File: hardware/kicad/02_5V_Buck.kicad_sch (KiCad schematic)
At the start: 9 parts

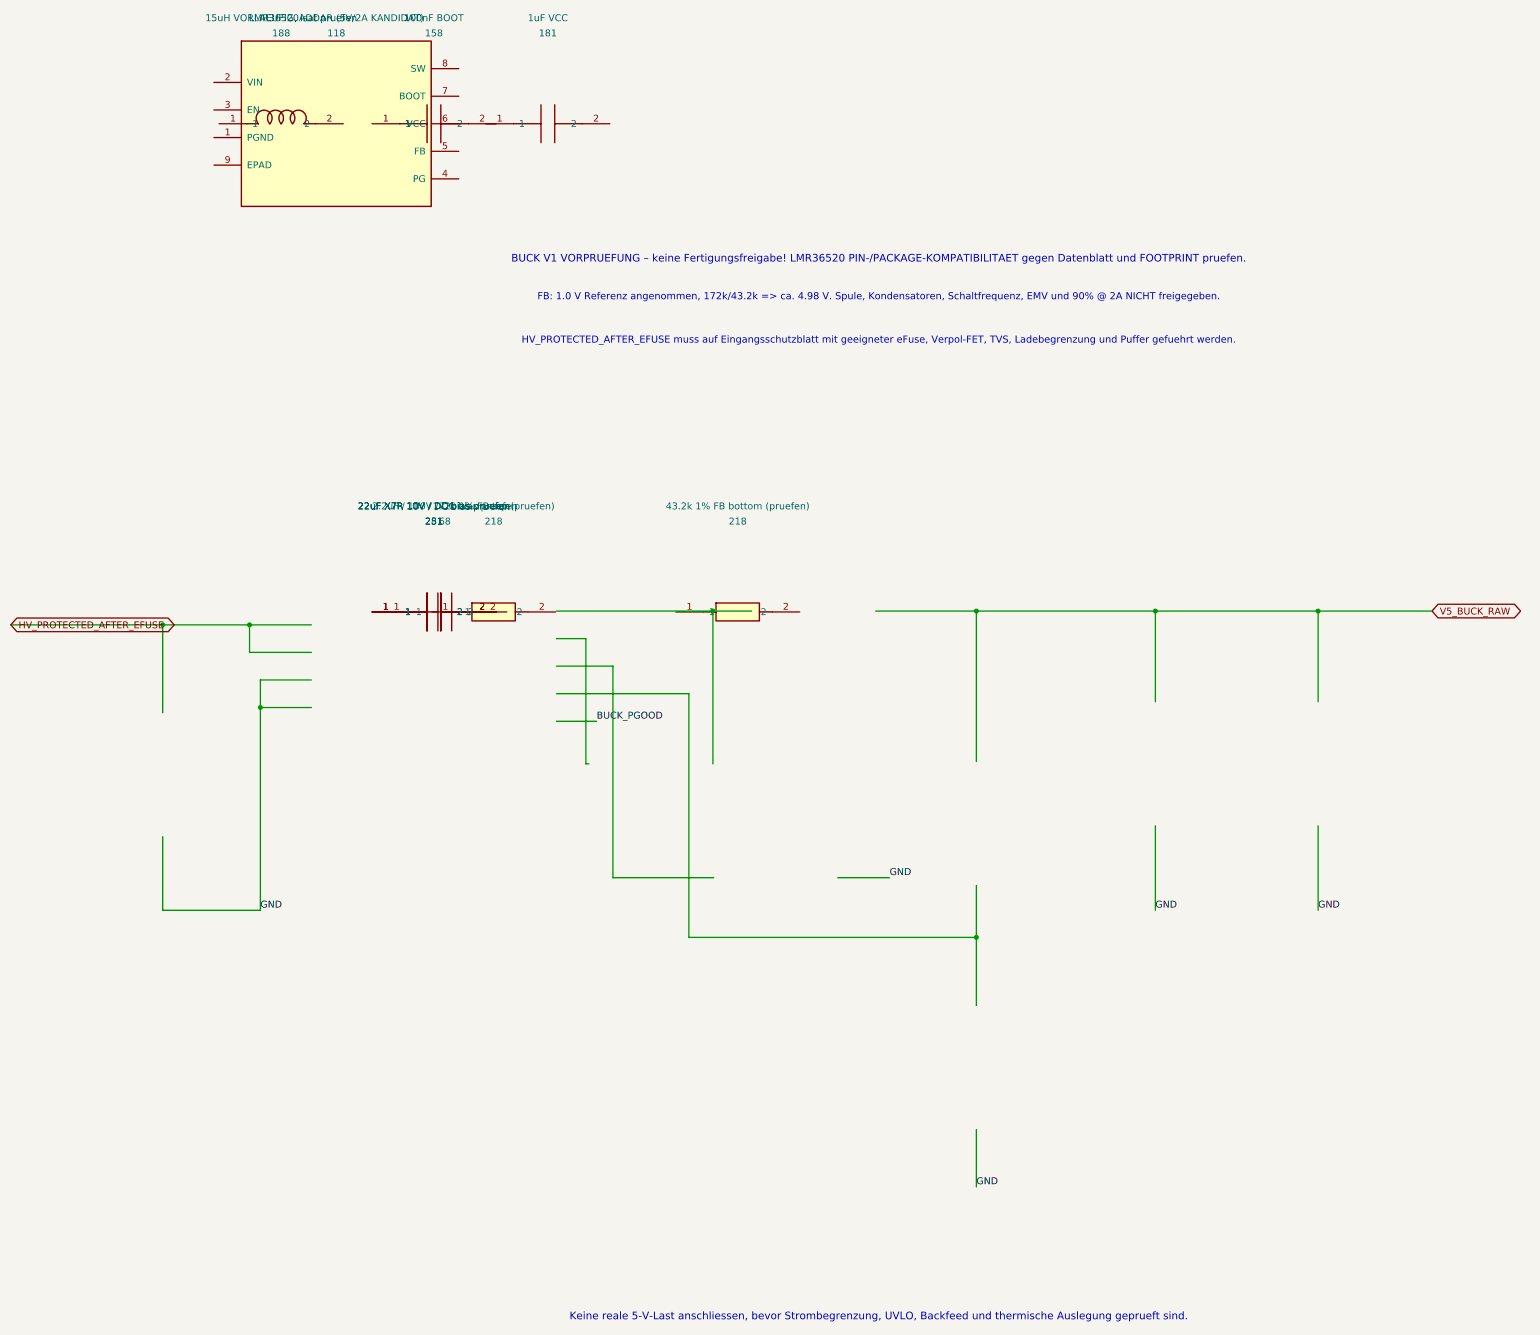
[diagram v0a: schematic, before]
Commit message: hardware: repair malformed buck symbol instances and validate references, positions and footprints
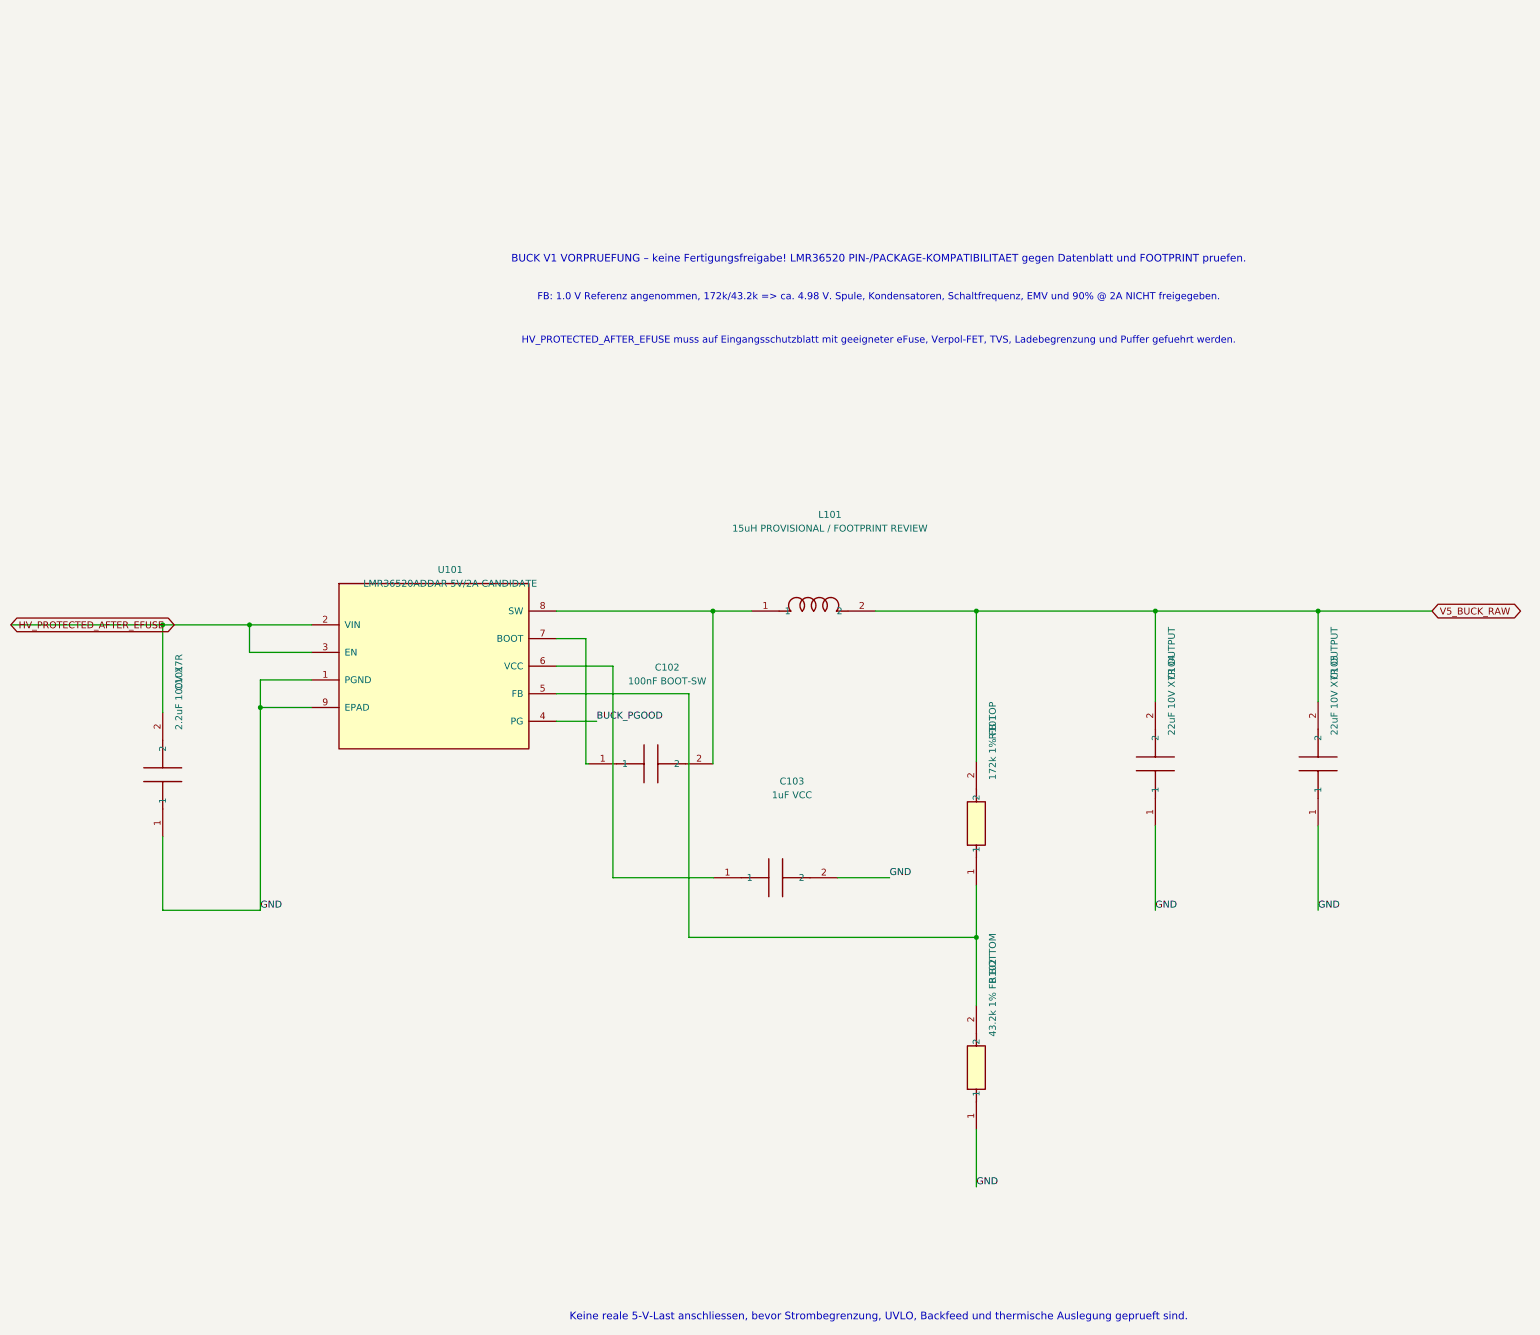
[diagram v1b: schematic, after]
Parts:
- C101: renamed from 2.2uF / 100V / DC bias pruefen; value 68 -> 2.2uF 100V X7R; footprint undefined -> Tripmaster:C_1210_3225
- C102: renamed from 100nF BOOT; value 158 -> 100nF BOOT-SW; footprint undefined -> Tripmaster:C_1206_3216
- C103: renamed from 1uF VCC; value 181 -> 1uF VCC; footprint undefined -> Tripmaster:C_1206_3216
- C104: renamed from 22uF X7R 10V / DC bias pruefen; value 251 -> 22uF 10V X7R OUTPUT; footprint undefined -> Tripmaster:C_1210_3225
- C105: renamed from 22uF X7R 10V / DC bias pruefen; value 281 -> 22uF 10V X7R OUTPUT; footprint undefined -> Tripmaster:C_1210_3225
- L101: renamed from 15uH VORLAEUFIG, Isat pruefen; value 188 -> 15uH PROVISIONAL / FOOTPRINT REVIEW; footprint undefined -> Tripmaster:L1_Bourns_SRN6045_220M
- R101: renamed from 172k 1% FB top (pruefen); value 218 -> 172k 1% FB TOP; footprint undefined -> Tripmaster:R_1206_3216
- R102: renamed from 43.2k 1% FB bottom (pruefen); value 218 -> 43.2k 1% FB BOTTOM; footprint undefined -> Tripmaster:R_1206_3216
- U101: renamed from LMR36520ADDAR (5V/2A KANDIDAT); value 118 -> LMR36520ADDAR 5V/2A CANDIDATE; footprint 1,2,3,4,5,6,7,8,9 -> Tripmaster:U3_TI_LMR36510ADDAR_DDA
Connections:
- net BUCK_PGOOD: now also U101.4 (PG)
- net GND: now also C101.1, C103.2, C104.1, C105.1, R102.1, U101.1 (PGND), U101.9 (EPAD)
- net HV_PROTECTED_AFTER_EFUSE: now also C101.2, U101.2 (VIN), U101.3 (EN)
- net V5_BUCK_RAW: now also C104.2, C105.2, L101.2, R101.2
- net at U101.5 (FB): now also R101.1, R102.2
- net at U101.6 (VCC): now also C103.1
- net at U101.7 (BOOT): now also C102.1
- net at U101.8 (SW): now also C102.2, L101.1
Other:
- moved on the sheet: C101, C102, C103, C104, C105, L101, R101, R102, U101
